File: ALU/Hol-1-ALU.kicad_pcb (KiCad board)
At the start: 2 copper layers, 109.2 x 78.7 mm, 29 parts, among them P1 REGISTER A LINK, P2 REGISTER B LINK, P3 STATUS & CTRL, P4 DATA BUS, P5 DATA BUS, P6 DATA BUS, P7 DATA BUS, P8 Power, U1 74LS283, U2 74LS283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

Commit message: v1.2.1 updated schematic and pcb pictures
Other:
- board text removed: "Data Bus"
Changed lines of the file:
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@@
     (area 82.857143 60.3504 195.630001 139.750001)
     (thickness 1.6)
-    (drawings 13)
+    (drawings 12)
     (tracks 443)
     (zones 0)
@@
     )
   )
-  (gr_text "Data Bus" (at 181.61 66.04) (layer F.SilkS)
-    (effects (font (size 1.5 1.5) (thickness 0.3)))
-  )
   (gr_text "Register A" (at 88.9 102.87 270) (layer F.SilkS)

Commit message: v1.3.6 silkscreen IC footprint corrections
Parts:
- U1, U2: footprint DIP-16__300 -> DIP-16
- U3, U4: footprint DIP-14__300 -> DIP-14
- U5, U6: footprint DIP-20__300 -> DIP-20
- moved C2 1.27 mm to (141.0, 100.3)
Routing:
- net GND: track 243.6 -> 242.7 mm
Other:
- board text added: "DATA BUS"
- board text added: "Gnd +5v"

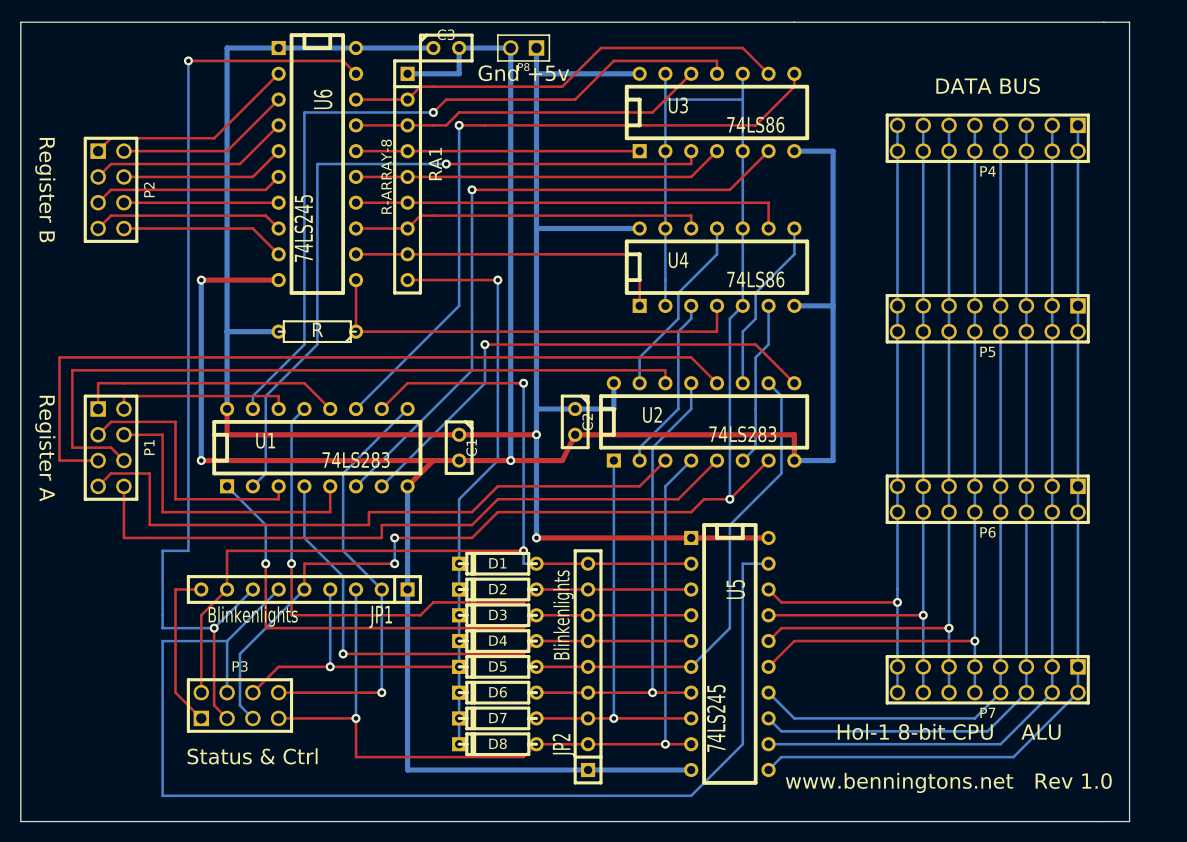
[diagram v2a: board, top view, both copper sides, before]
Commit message: v1.5.15 ALU: Re-numbered 8 pin IDC ports to reflect the anti-clockwise numbering used
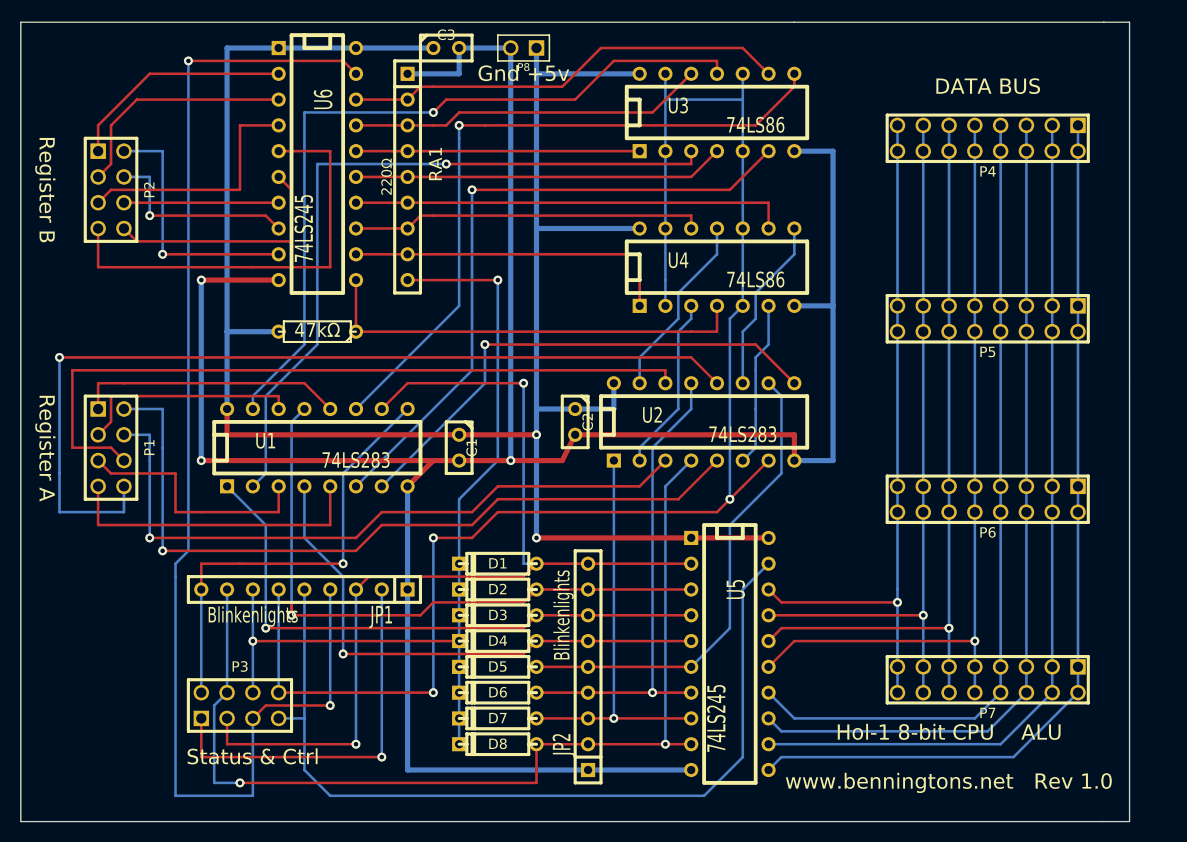
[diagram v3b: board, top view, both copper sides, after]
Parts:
- R1: value R -> 47kΩ
- RA1: value R-ARRAY-8 -> 220Ω
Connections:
- JP1 pad 2: /Carry? -> N-0000035
- JP1 pad 3: /Odd? -> /Negative?
- JP1 pad 4: /Not Zero? -> /INC
- JP1 pad 5: /Subtract -> /Sum Out
- JP1 pad 6: /Sum Out -> /Subtract
- JP1 pad 7: /INC -> /Not Zero?
- JP1 pad 8: /Negative? -> /Odd?
- JP1 pad 9: N-0000040 -> /Carry?
- P1 pad 2: /A7 -> /A1
- P1 pad 3: /A6 -> /A7
- P1 pad 4: /A5 -> /A2
- P1 pad 5: /A4 -> /A6
- P1 pad 7: /A2 -> /A5
- P1 pad 8: /A1 -> /A4
- P2 pad 2: N-0000034 -> N-0000030
- P2 pad 3: N-0000035 -> N-0000036
- P2 pad 4: N-0000036 -> N-0000037
- P2 pad 5: N-0000032 (its old number) -> N-0000038
- P2 pad 7: N-0000038 -> N-0000029
- P2 pad 8: N-0000039 (its old number) -> N-0000034
- P3 pad 1: N-0000040 -> N-0000035
- P3 pad 2: /Negative? -> /Carry?
- P3 pad 3: /INC -> /Negative?
- P3 pad 4: /Sum Out -> /Odd?
- P3 pad 5: /Subtract -> /INC
- P3 pad 7: /Odd? -> /Sum Out
- P3 pad 8: /Carry? -> /Subtract
- U6 pad 3: N-0000034 -> N-0000036
- U6 pad 4: N-0000035 -> N-0000038
- U6 pad 5: N-0000036 -> N-0000029
- U6 pad 6: N-0000032 (its old number) -> N-0000034
- U6 pad 8: N-0000038 -> N-0000037
- U6 pad 9: N-0000039 (its old number) -> N-0000030
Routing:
- net N-0000029: track 0.00 -> 43.2 mm
- net /INC: track 95.3 -> 124.8 mm
- net /Sum Out: track 113.4 -> 86.2 mm
- net N-0000030: track 0.00 -> 25.4 mm, vias 0 -> 1
- net N-0000037: track 0.00 -> 19.6 mm, vias 0 -> 1
- net N-0000032 (its old number): track 18.8 -> 0.00 mm
- net N-0000035: track 19.9 -> 38.1 mm, vias 0 -> 1
- net N-0000040: track 16.3 -> 0.00 mm
- net N-0000039 (its old number): track 16.3 -> 0.00 mm
- net /Odd?: track 86.7 -> 99.4 mm
- net /A4: track 79.8 -> 90.0 mm, vias 0 -> 1
- net /A1: track 67.4 -> 76.1 mm, vias 0 -> 1
- net /Subtract: track 142.7 -> 149.7 mm
- net N-0000036: track 16.3 -> 23.2 mm
- net N-0000034: track 17.3 -> 23.9 mm
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
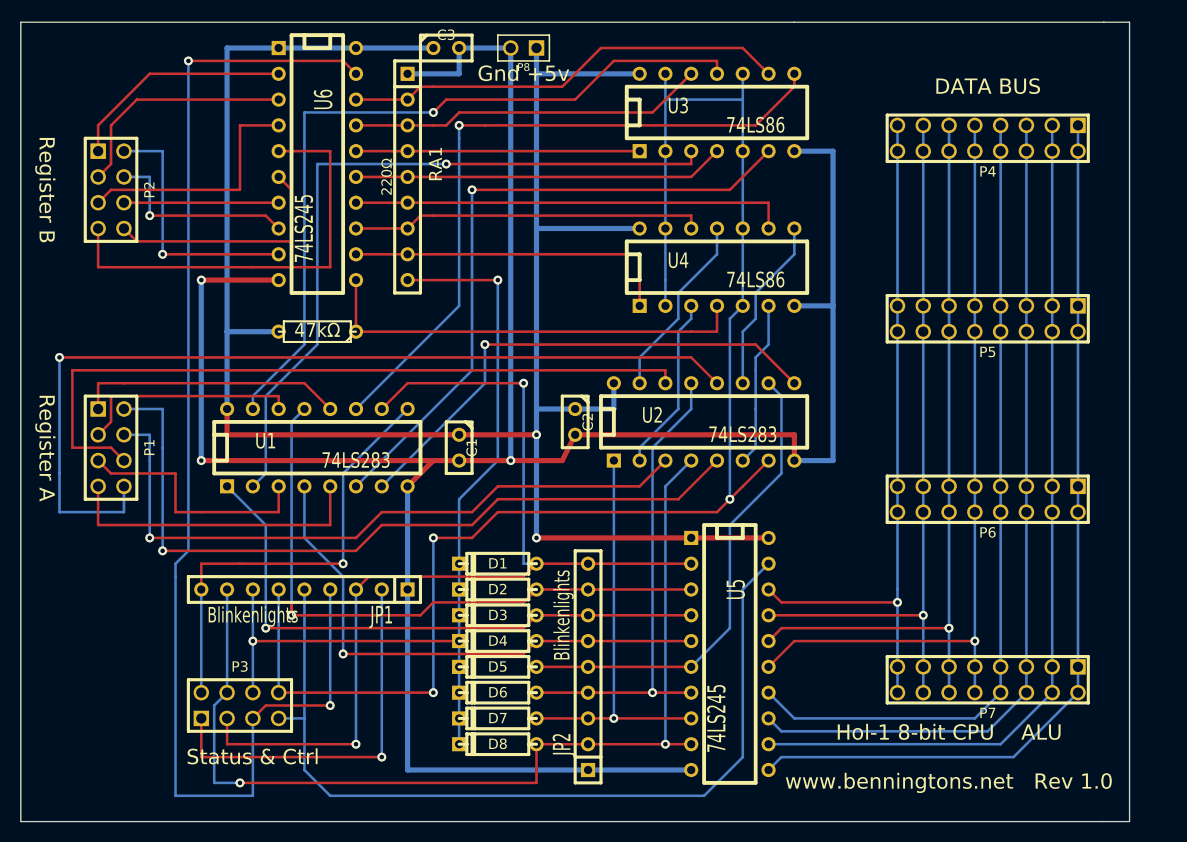
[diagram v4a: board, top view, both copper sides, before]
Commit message: 1.5.21 upgraded to KiCad 6.0
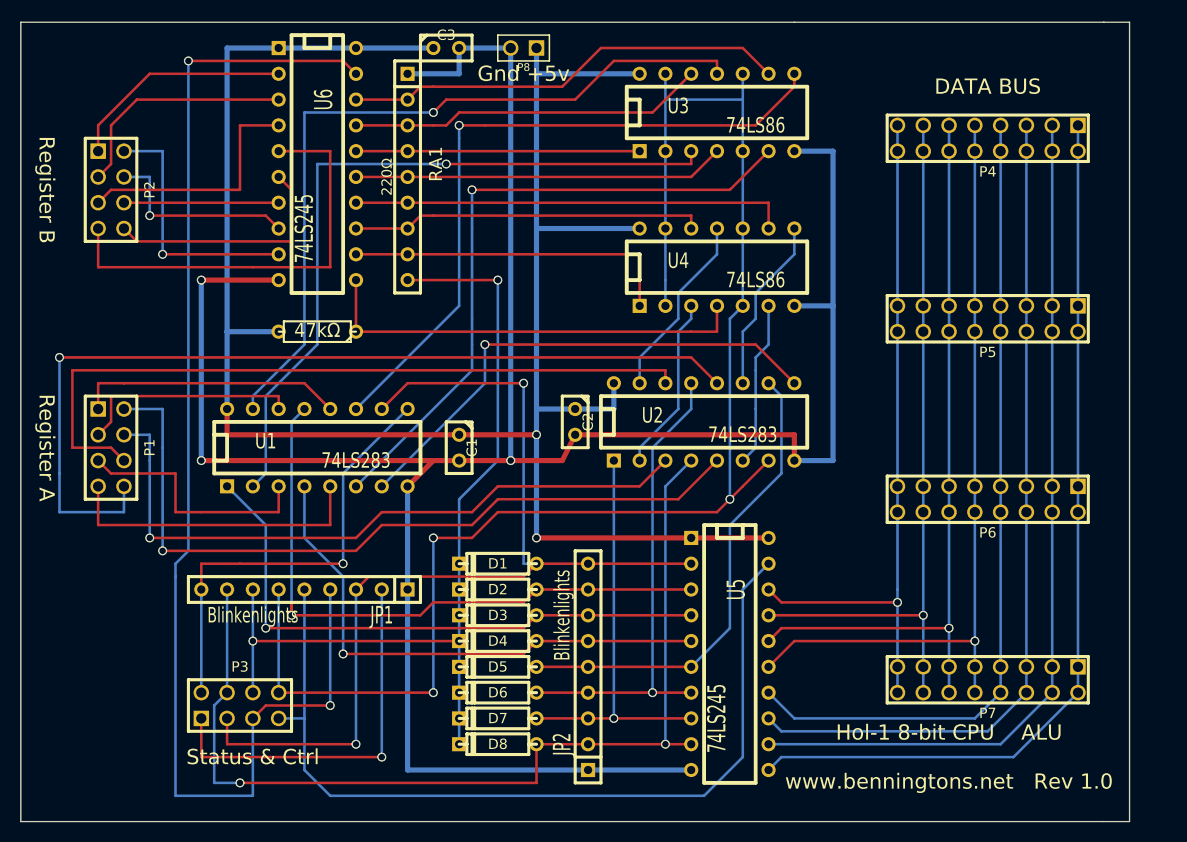
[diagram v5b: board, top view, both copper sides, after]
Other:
- net class Default removed
